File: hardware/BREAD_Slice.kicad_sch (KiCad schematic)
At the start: 22 parts, among them J1 Conn_01x10_Female

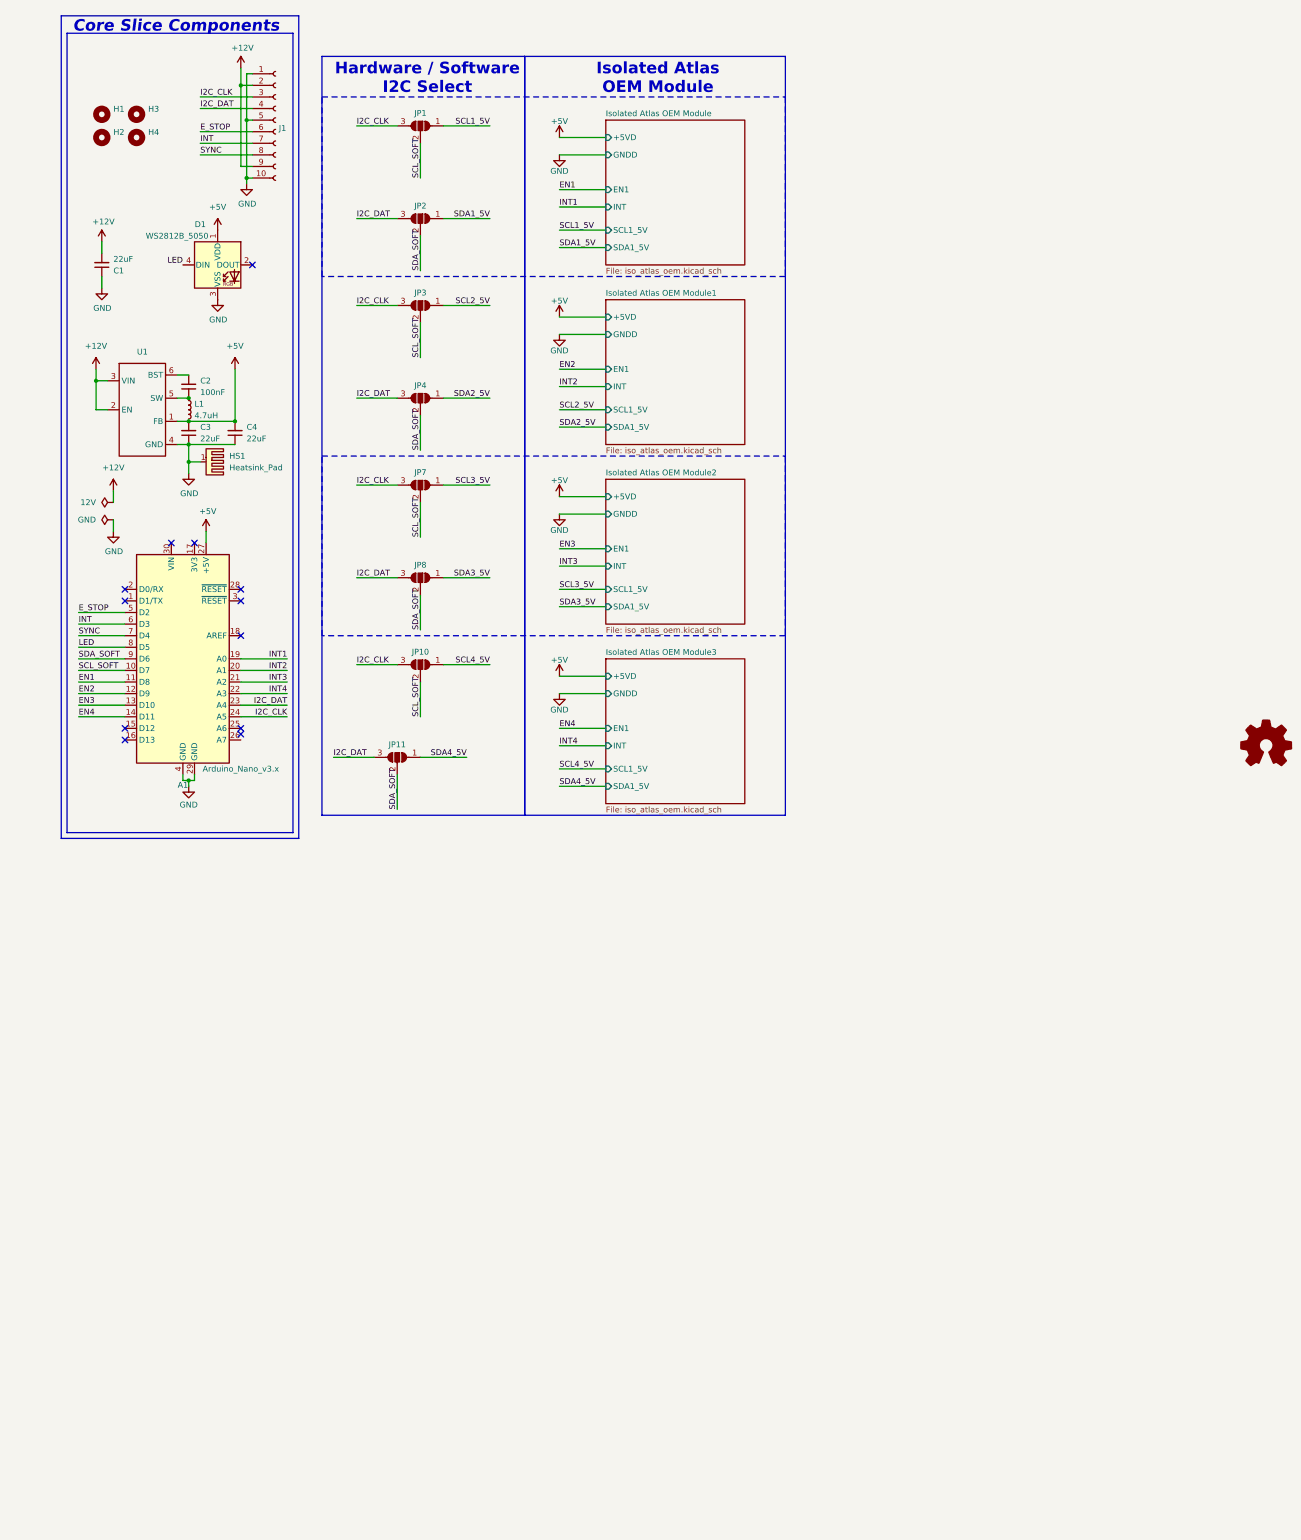
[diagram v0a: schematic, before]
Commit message: removed legacy folders
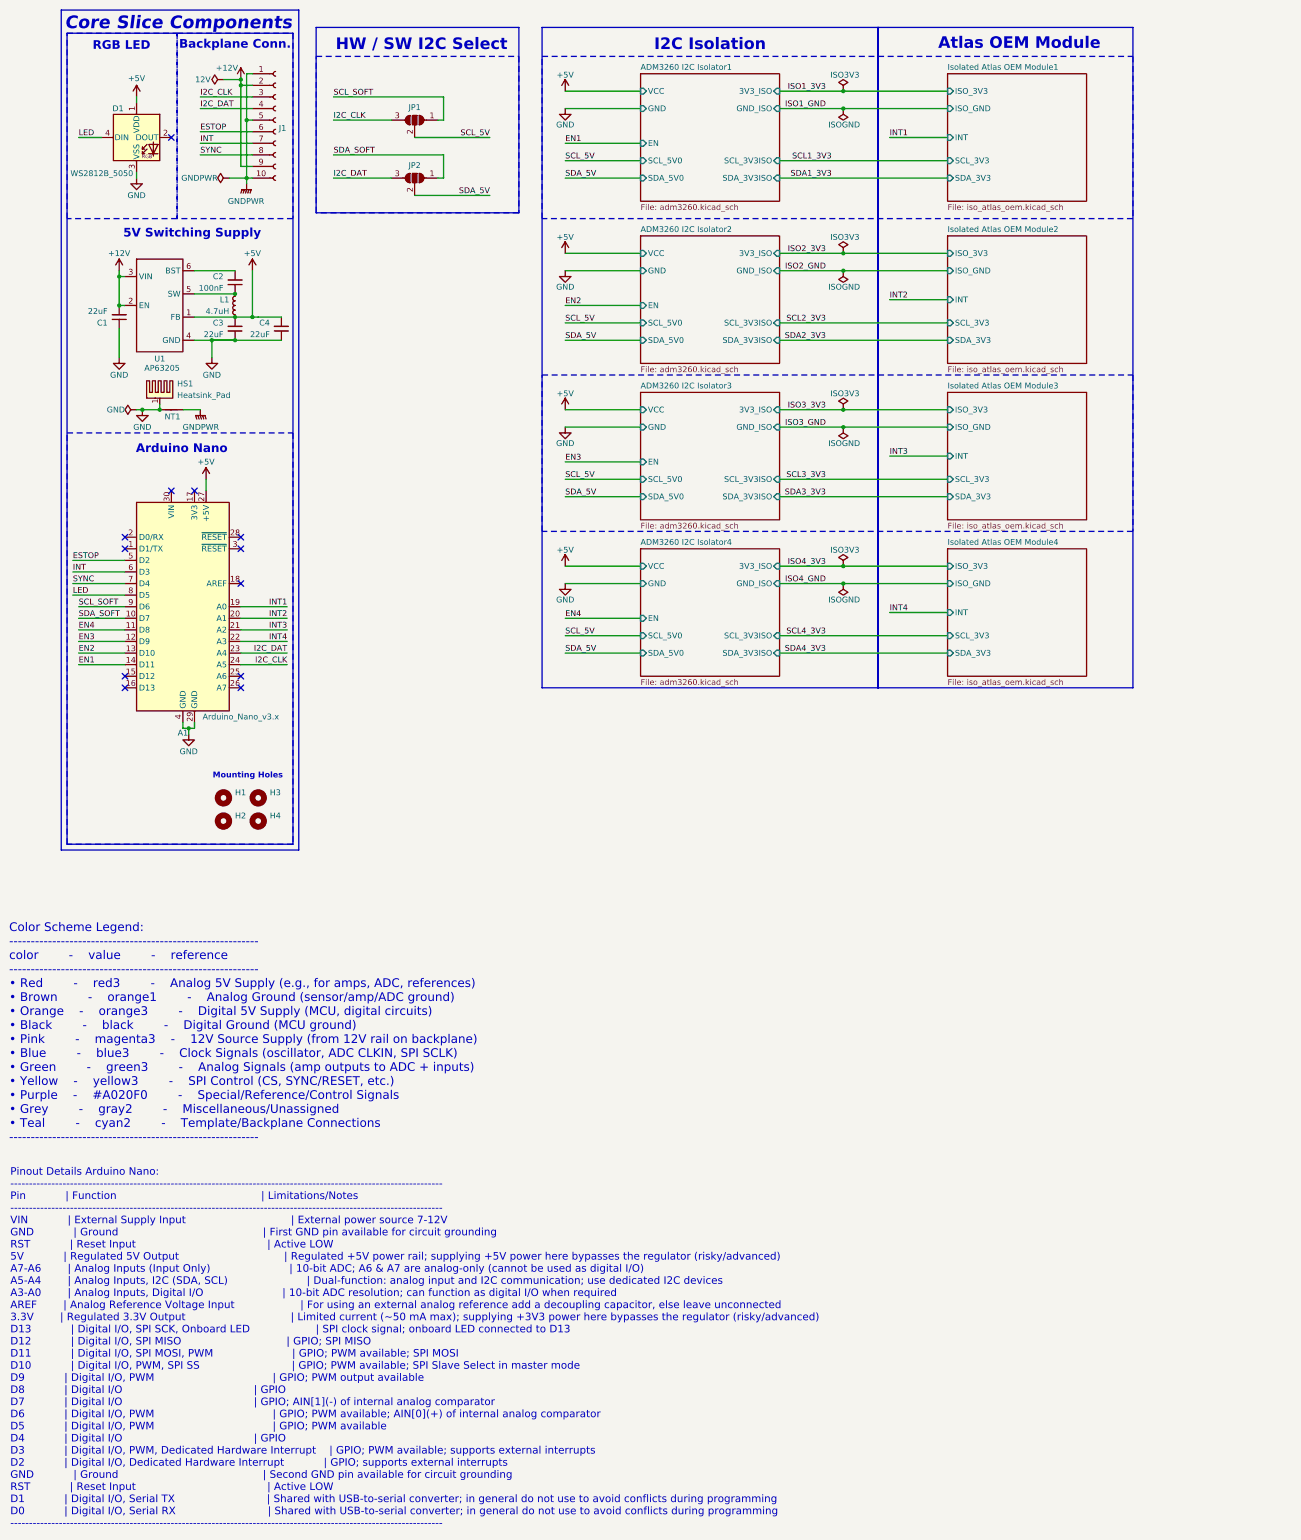
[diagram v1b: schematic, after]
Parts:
- removed JP10, JP11, JP3, JP4, JP7, JP8: SolderJumper_3_Open, Jumper:SolderJumper-3_P1.3mm_Open_RoundedPad1.0x1.5mm, symbol Jumper:SolderJumper_3_Open
- added NT1: NetTie_2, NetTie:NetTie-2_SMD_Pad2.0mm, symbol Device:NetTie_2
- D1: PROD_ID (none) -> DIO-12503
- U1: value ~ -> AP63205
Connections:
- net SCL1_5V is gone; now on net SCL_SOFT: JP1.1 (A)
- net SDA1_5V is gone; now on net SDA_SOFT: JP2.1 (A)
- net EN1: now also A1.14 (D11); no longer A1.11 (D8)
- net EN2: now also A1.13 (D10); no longer A1.12 (D9)
- net EN3: now also A1.12 (D9); no longer A1.13 (D10)
- net EN4: now also A1.11 (D8); no longer A1.14 (D11)
- net GND: now also NT1.1; no longer J1.1 (Pin_1), J1.10 (Pin_10), J1.5 (Pin_5)
- net SCL_SOFT: now also A1.9 (D6); no longer A1.10 (D7), JP1.2 (C)
- net SDA_SOFT: now also A1.10 (D7); no longer A1.9 (D6), JP2.2 (C)
- net E_STOP renamed ESTOP
- new net GNDPWR: J1.1 (Pin_1), J1.10 (Pin_10), J1.5 (Pin_5), NT1.2
- new net SCL_5V: JP1.2 (C)
- new net SDA_5V: JP2.2 (C)
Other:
- removed sheet Isolated Atlas OEM Module
- added sheet ADM3260 I2C Isolator1 (adm3260.kicad_sch)
- added sheet ADM3260 I2C Isolator2 (adm3260.kicad_sch)
- added sheet ADM3260 I2C Isolator3 (adm3260.kicad_sch)
- added sheet ADM3260 I2C Isolator4 (adm3260.kicad_sch)
- added sheet Isolated Atlas OEM Module4 (iso_atlas_oem.kicad_sch)
- sheet Isolated Atlas OEM Module1 ports: added ISO_3V3, ISO_GND, SCL_3V3, SDA_3V3; removed +5VD, EN1, GNDD, SCL1_5V, SDA1_5V
- sheet Isolated Atlas OEM Module2 ports: added ISO_3V3, ISO_GND, SCL_3V3, SDA_3V3; removed +5VD, EN1, GNDD, SCL1_5V, SDA1_5V
- sheet Isolated Atlas OEM Module3 ports: added ISO_3V3, ISO_GND, SCL_3V3, SDA_3V3; removed +5VD, EN1, GNDD, SCL1_5V, SDA1_5V
- note added: "5V Switching Supply"
- note added: "Arduino Nano"
- note added: "Atlas OEM Module"
- note added: "Backplane Conn."
- note added: "Color Scheme Legend: ---------------------------------------------------------- color - value - reference ---------------------------------------------------------- • Red - red3 - Analog 5V Supply (e.g., for amps, ADC, references) • Brown - orange1 - Analog Ground (sensor/amp/ADC ground) • Orange - orange3 - Digital 5V Supply (MCU, digital circuits) • Black - black - Digital Ground (MCU ground) •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"
- note added: "HW / SW I2C Select"
- note added: "I2C Isolation"
- note added: "Mounting Holes"
- note added: "Pinout Details Arduino Nano: -------------------------------------------------------------------------------------------------------------------- Pin | Function | Limitations/Notes -------------------------------------------------------------------------------------------------------------------- VIN | External Supply Input | External power source 7-12V GND | Ground | First GND pin available for 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"
- note added: "RGB LED"
- note removed: "Hardware / Software I2C Select"
- note removed: "Isolated Atlas OEM Module"
- moved on the sheet: A1, C1, C2, C3, C4, H1, H2, H3, H4, JP1, JP2, L1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
